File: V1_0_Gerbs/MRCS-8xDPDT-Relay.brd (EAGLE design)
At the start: 150 x 70 mm, 20 parts, among them CON1 CONNECTOR-M10LOCK, IC1 ULN2830, K1 RELAY-G2R2, K2 RELAY-G2R2, K3 RELAY-G2R2, K4 RELAY-G2R2, K5 RELAY-G2R2, K6 RELAY-G2R2, K7 RELAY-G2R2, K8 RELAY-G2R2

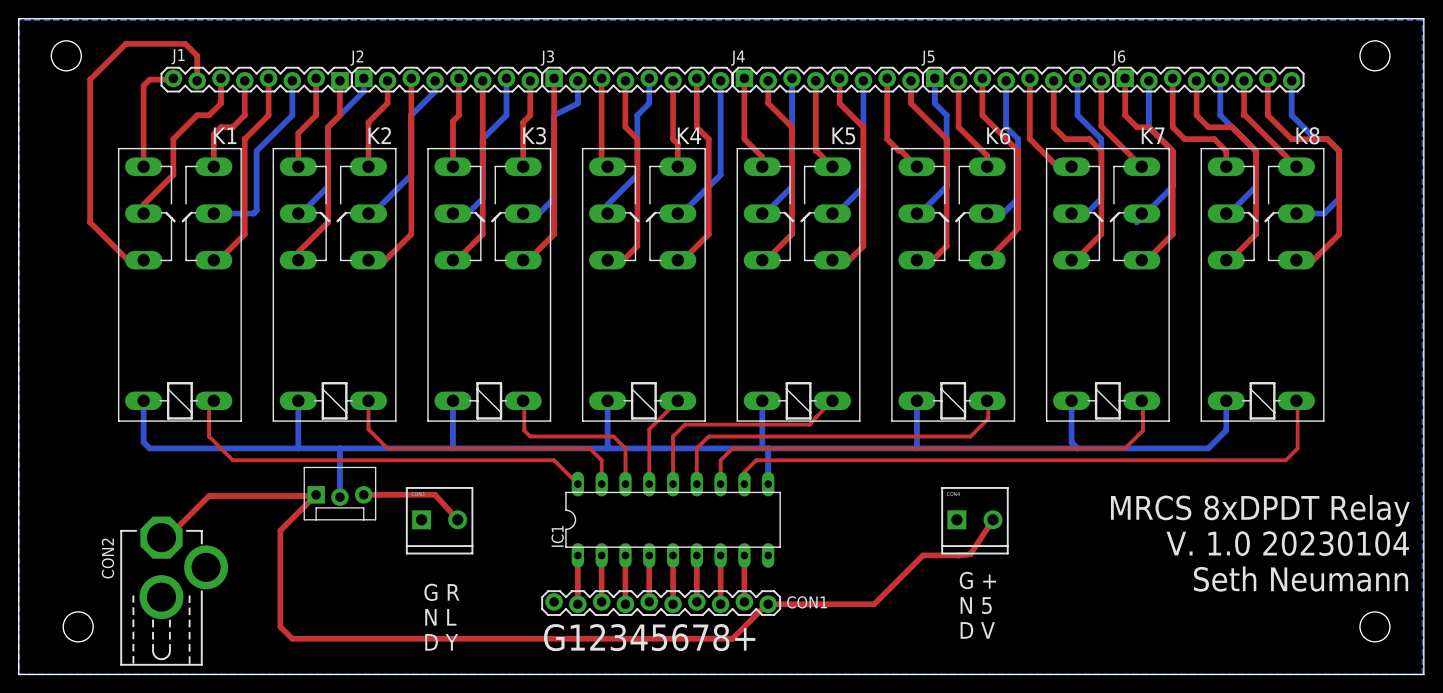
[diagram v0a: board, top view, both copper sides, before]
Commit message: first release send out for fab
this was sent out for fab. First release is for test.
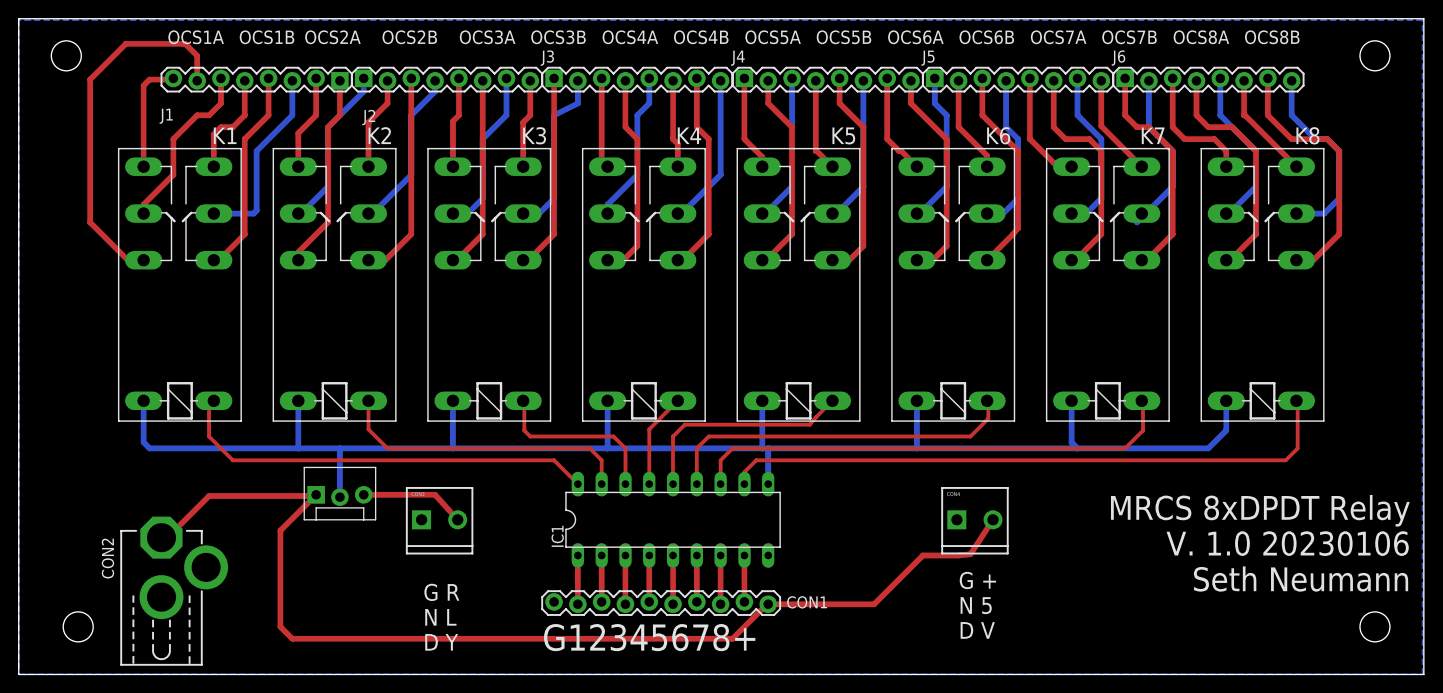
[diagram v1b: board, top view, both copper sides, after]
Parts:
- added U$1: (no value), MRCS-prop65warningBtm:CA-PROP65WARNING
- added U$2: (no value), MRCSLogoBtm:MRCSLOGOBTM
- added U$3: (no value), MRCSLogoTop:MRCSLOGOTOP
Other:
- board text added: "MRCS 8xDPDT Relay V. 1.0 20230106 Seth Neumann"
- board text added: "OCS1A"
- board text added: "OCS1B"
- board text added: "OCS2A"
- board text added: "OCS2B"
- board text added: "OCS3A"
- board text added: "OCS3B"
- board text added: "OCS4A"
- board text added: "OCS4B"
- board text added: "OCS5A"
- board text added: "OCS5B"
- board text added: "OCS6A"
- board text added: "OCS6B"
- board text added: "OCS7A"
- board text added: "OCS7B"
- board text added: "OCS8A"
- board text added: "OCS8B"
- board text removed: "MRCS 8xDPDT Relay V. 1.0 20230104 Seth Neumann"
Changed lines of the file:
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@@
 D Y</text>
 <text x="148.59" y="19.05" size="2.54" layer="21" font="vector" ratio="10" rot="R180">MRCS 8xDPDT Relay
-V. 1.0 20230104
+V. 1.0 20230106
 Seth Neumann</text>
 <hole x="5.08" y="66.04" drill="3.2"/>
@@
 <hole x="144.78" y="5.08" drill="3.2"/>
 <hole x="144.78" y="66.04" drill="3.2"/>
+<text x="15.875" y="67.31" size="1.4224" layer="21" font="vector" ratio="10">OCS1A</text>
+<text x="23.495" y="67.31" size="1.4224" layer="21" font="vector" ratio="10">OCS1B</text>
+<text x="30.48" y="67.31" size="1.4224" layer="21" font="vector" ratio="10">OCS2A</text>
+<text x="38.735" y="67.31" size="1.4224" layer="21" font="vector" ratio="10">OCS2B</text>
+<text x="46.99" y="67.31" size="1.4224" layer="21" font="vector" ratio="10">OCS3A</text>
+<text x="54.61" y="67.31" size="1.4224" layer="21" font="vector" ratio="10">OCS3B</text>
+<text x="62.23" y="67.31" size="1.4224" layer="21" font="vector" ratio="10">OCS4A</text>
+<text x="69.85" y="67.31" size="1.4224" layer="21" font="vector" ratio="10">OCS4B</text>
+<text x="77.47" y="67.31" size="1.4224" layer="21" font="vector" ratio="10">OCS5A</text>
+<text x="85.09" y="67.31" size="1.4224" layer="21" font="vector" ratio="10">OCS5B</text>
+<text x="92.71" y="67.31" size="1.4224" layer="21" font="vector" ratio="10">OCS6A</text>
+<text x="100.33" y="67.31" size="1.4224" layer="21" font="vector" ratio="10">OCS6B</text>
+<text x="107.95" y="67.31" size="1.4224" layer="21" font="vector" ratio="10">OCS7A</text>
+<text x="115.57" y="67.31" size="1.4224" layer="21" font="vector" ratio="10">OCS7B</text>
+<text x="123.19" y="67.31" size="1.4224" layer="21" font="vector" ratio="10">OCS8A</text>
+<text x="130.81" y="67.31" size="1.4224" layer="21" font="vector" ratio="10">OCS8B</text>
 </plain>
 <attributes>
@@
 <element name="IC1" library="MRCS" package="DIL18" value="ULN2830" x="69.85" y="16.51"/>
 <element name="J1" library="SPCoast" package="1X08_LOCK" value="" x="34.29" y="63.5" smashed="yes" rot="R180">
-<attribute name="NAME" x="17.8562" y="66.7512" size="1.27" layer="25" ratio="10" rot="R180"/>
+<attribute name="NAME" x="16.5862" y="60.4012" size="1.27" layer="25" ratio="10" rot="R180"/>
 <attribute name="VALUE" x="35.56" y="66.675" size="1.27" layer="27" rot="R180"/>
 </element>
 <element name="J2" library="SPCoast" package="1X08_LOCK" value="" x="36.83" y="63.5" smashed="yes">
-<attribute name="NAME" x="35.4838" y="65.3288" size="1.27" layer="25" ratio="10"/>
+<attribute name="NAME" x="36.7538" y="58.9788" size="1.27" layer="25" ratio="10"/>
 <attribute name="VALUE" x="35.56" y="60.325" size="1.27" layer="27"/>
 </element>
@@
 <element name="CON4" library="SPCoast" package="SCREWTERMINAL-3.5MM-2_LOCK" value="" x="100.33" y="16.51"/>
 <element name="RELAY_PWR" library="SPCoast" package="MOLEX-1X3_LOCK" value="CONNECTOR-M03MOLEX-254-LOCK" x="31.75" y="19.05"/>
+<element name="U$1" library="MRCS-prop65warningBtm" package="CA-PROP65WARNING" value="" x="109.22" y="8.89"/>
+<element name="U$2" library="MRCSLogoBtm" package="MRCSLOGOBTM" value="" x="132.08" y="13.97"/>
+<element name="U$3" library="MRCSLogoTop" package="MRCSLOGOTOP" value="" x="2.54" y="19.05"/>
 </elements>
 <signals>
